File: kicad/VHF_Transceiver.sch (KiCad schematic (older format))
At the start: 16 parts

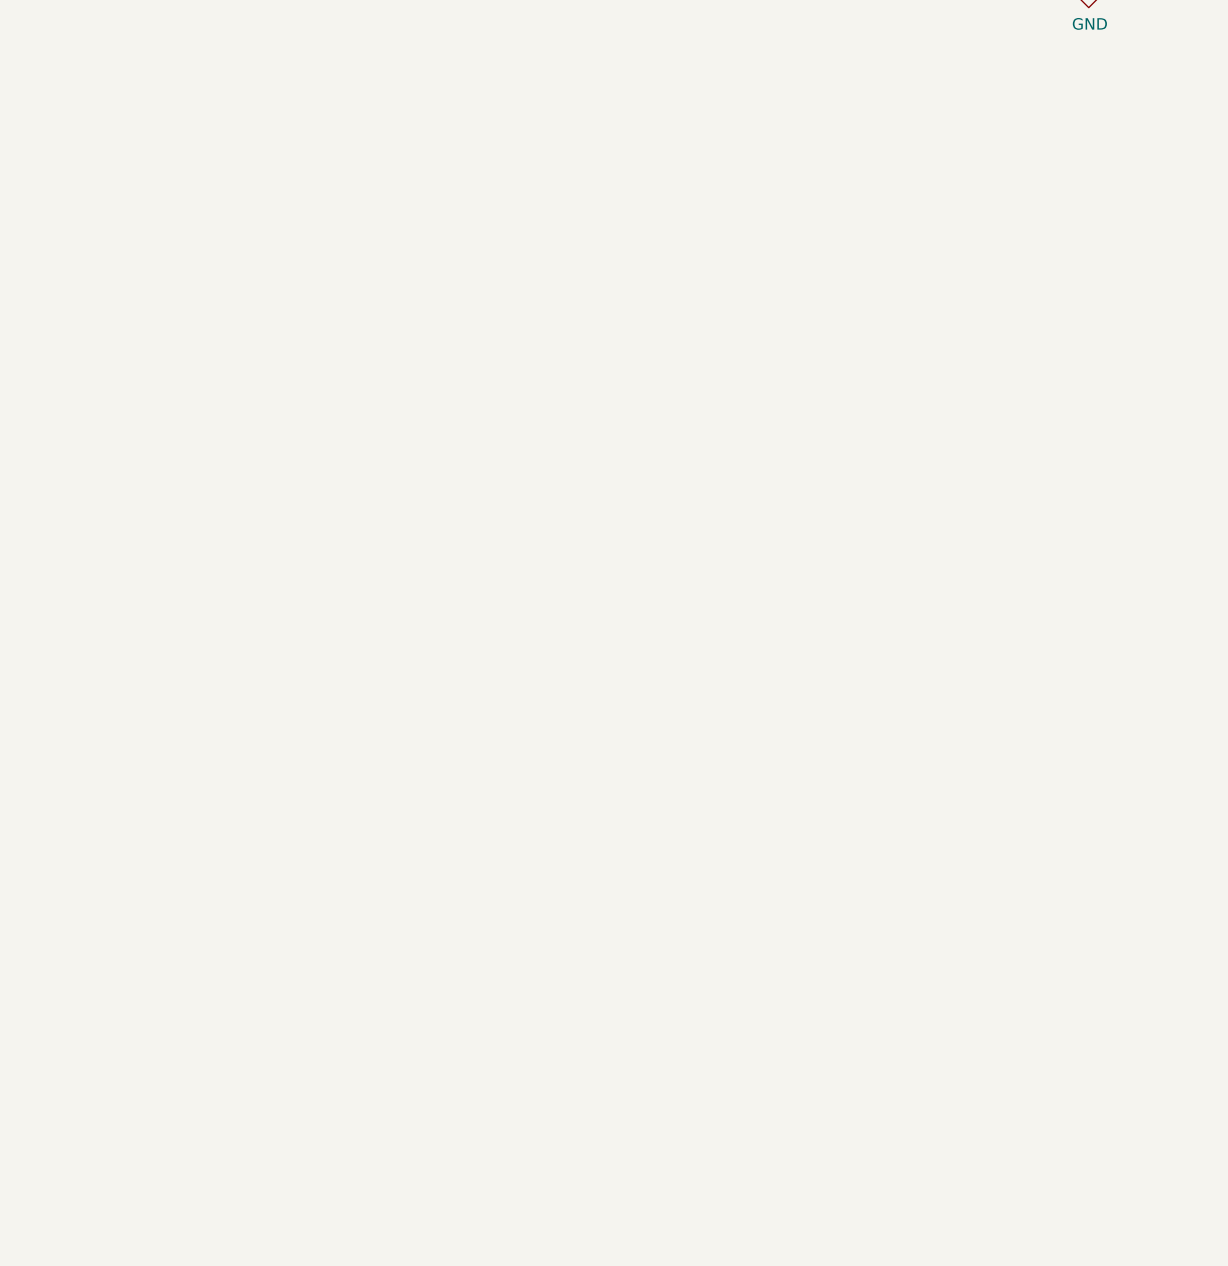
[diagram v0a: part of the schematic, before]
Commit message: New rx-tx bidirectional amplifier
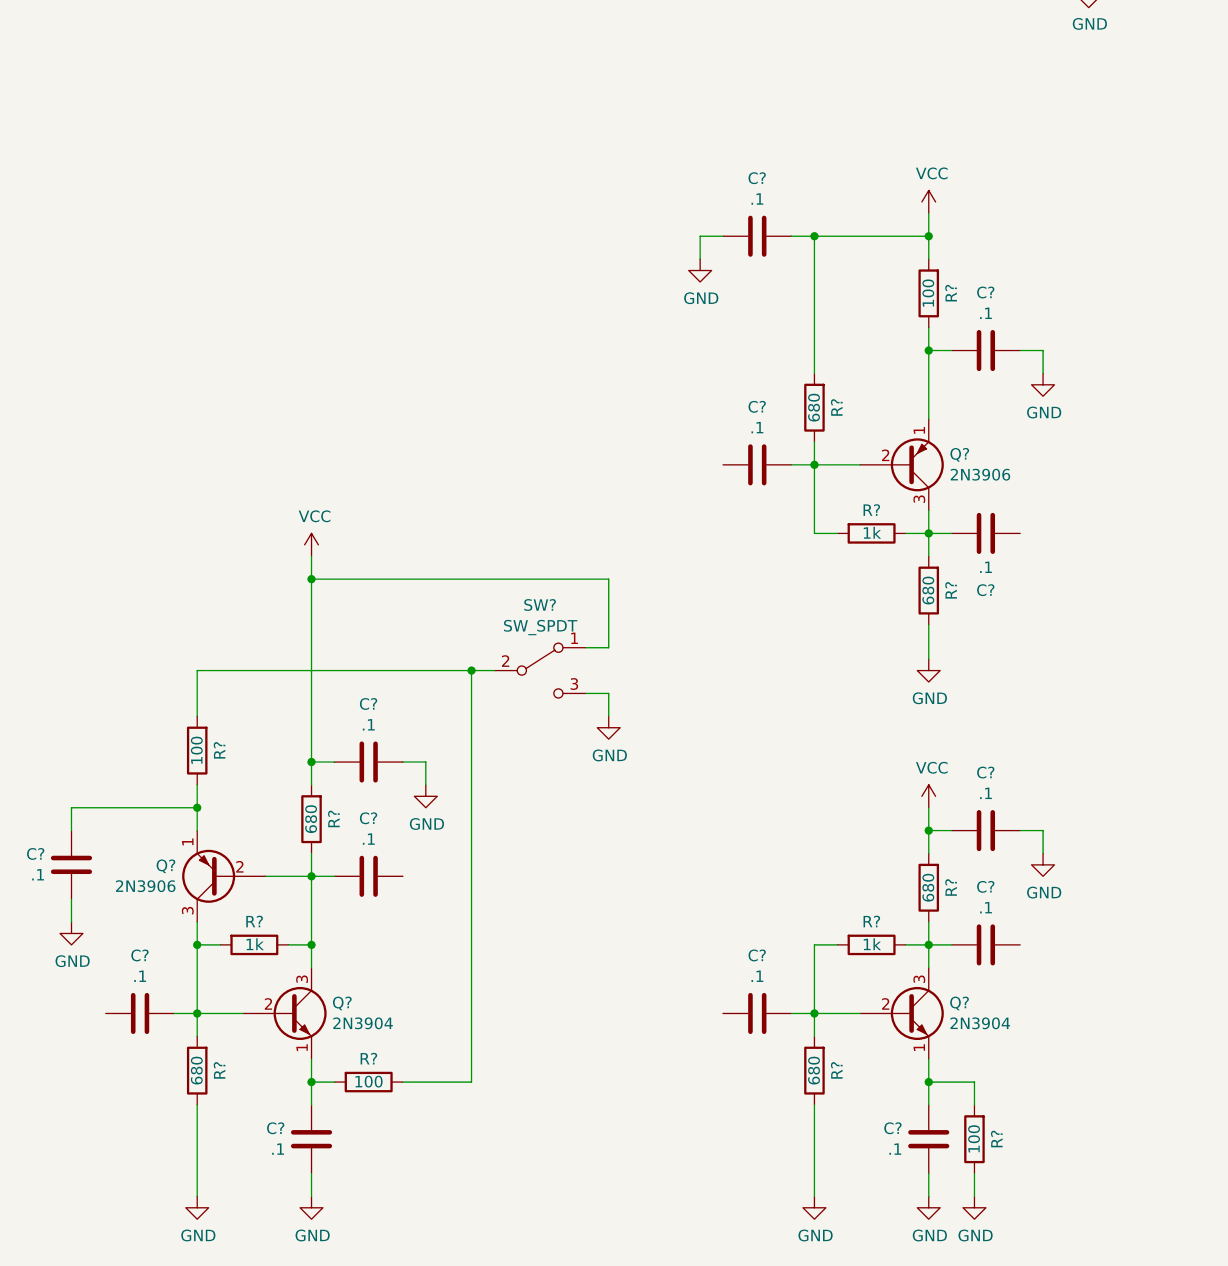
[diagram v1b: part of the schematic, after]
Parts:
- added C? (x13): .1, symbol device:C
- added Q? (x2): 2N3904, TO_SOT_Packages_THT:TO-92_Molded_Narrow, symbol transistors:2N3904
- added Q? (x2): 2N3906, TO_SOT_Packages_THT:TO-92_Molded_Narrow, symbol transistors:2N3906
- added R? (x3): 1k, symbol device:R
- added R? (x6): 680, symbol device:R
- added R? (x4): 100, symbol device:R
- added SW?: SW_SPDT, symbol switches:SW_SPDT
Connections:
- net GND: now also C?.1, C?.1, C?.1, C?.1, C?.2, C?.2, C?.2, R?.1, R?.1, R?.1, R?.1, SW?.3 (C)
- net VCC: now also C?.1, C?.1, C?.2, R?.2, R?.2, R?.2, R?.2, SW?.1 (A)
- new net: C?.2, Q?.1 (E), R?.2 (x2)
- new net: C?.2, Q?.2 (B), Q?.3 (C), R?.2, R?.2
- new net: C?.1, Q?.2 (B), Q?.3 (C), R?.1, R?.1
- new net: C?.2, Q?.1 (E), R?.1
- new net: R?.1, R?.2, SW?.2 (B)
- new net: C?.1, Q?.1 (E), R?.1
- new net: C?.2, Q?.2 (B), R?.1, R?.2
- new net: C?.2, Q?.3 (C), R?.1, R?.2
- new net: C?.2, Q?.2 (B), R?.2, R?.2
- new net: C?.1, Q?.3 (C), R?.1, R?.1
